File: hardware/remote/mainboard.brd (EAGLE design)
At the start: 34.7 x 20.3 mm, 11 parts, among them J1 AVR_SPI_PRG_6PTH, U1 ATMEGA328P_VQFNVQFN, U2 RFM69HCW

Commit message: Preliminary PCB design
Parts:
- J1: value AVR_SPI_PRG_6PTH -> (none)
- moved C2 11.5 mm to (23.9, 1.52), turned to 180 degrees
- moved C1 10.2 mm to (1.52, 9.65), turned to 270 degrees
- moved R2 5.43 mm to (14.2, 8.13), turned to 90 degrees
- moved C3 1.37 mm to (5.33, 9.65)
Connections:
- removed net N$3: C2.2, U2.10, U2.8
- net GND: now also C2.2, U2.10, U2.8
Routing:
- net VCC: track 0.00 -> 96.7 mm, vias 0 -> 2
- net N$6: track 0.00 -> 38.8 mm, vias 0 -> 4
- net MOSI: track 0.00 -> 33.7 mm, vias 0 -> 2
- net SCK: track 0.00 -> 28.3 mm, vias 0 -> 1
- net N$8: track 0.00 -> 27.9 mm, vias 0 -> 2
- net N$1: track 0.00 -> 20.0 mm
- net MISO: track 0.00 -> 17.0 mm
- net N$2: track 0.00 -> 9.32 mm
- net N$4: track 0.00 -> 2.70 mm
- added copper zone on layer 1, net GND
- added copper zone on layer 16, net GND

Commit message: Added BOM and modified resistor value
Remote
* Added detailed BOM with digikey part numbers.
* Changed R2 from 50k to 47k as 47k is a much more common value.
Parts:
- R2: value 50k -> 47k
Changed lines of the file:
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@@
 <element name="J1" library="SparkFun-Connectors" package="2X3" value="" x="5.08" y="12.7" rot="R90"/>
 <element name="R1" library="SparkFun-Passives" package="0603-RES" value="10k" x="8.128" y="19.05" rot="R180"/>
-<element name="R2" library="SparkFun-Passives" package="0603-RES" value="50k" x="14.224" y="8.128" rot="R90"/>
+<element name="R2" library="SparkFun-Passives" package="0603-RES" value="47k" x="14.224" y="8.128" rot="R90"/>
 <element name="S1" library="SparkFun-Electromechanical" package="TACTILE-PTH" value="" x="4.572" y="4.064">
 <attribute name="PROD_ID" value=" SWCH-08441" x="4.572" y="4.064" size="1.778" layer="27" display="off"/>

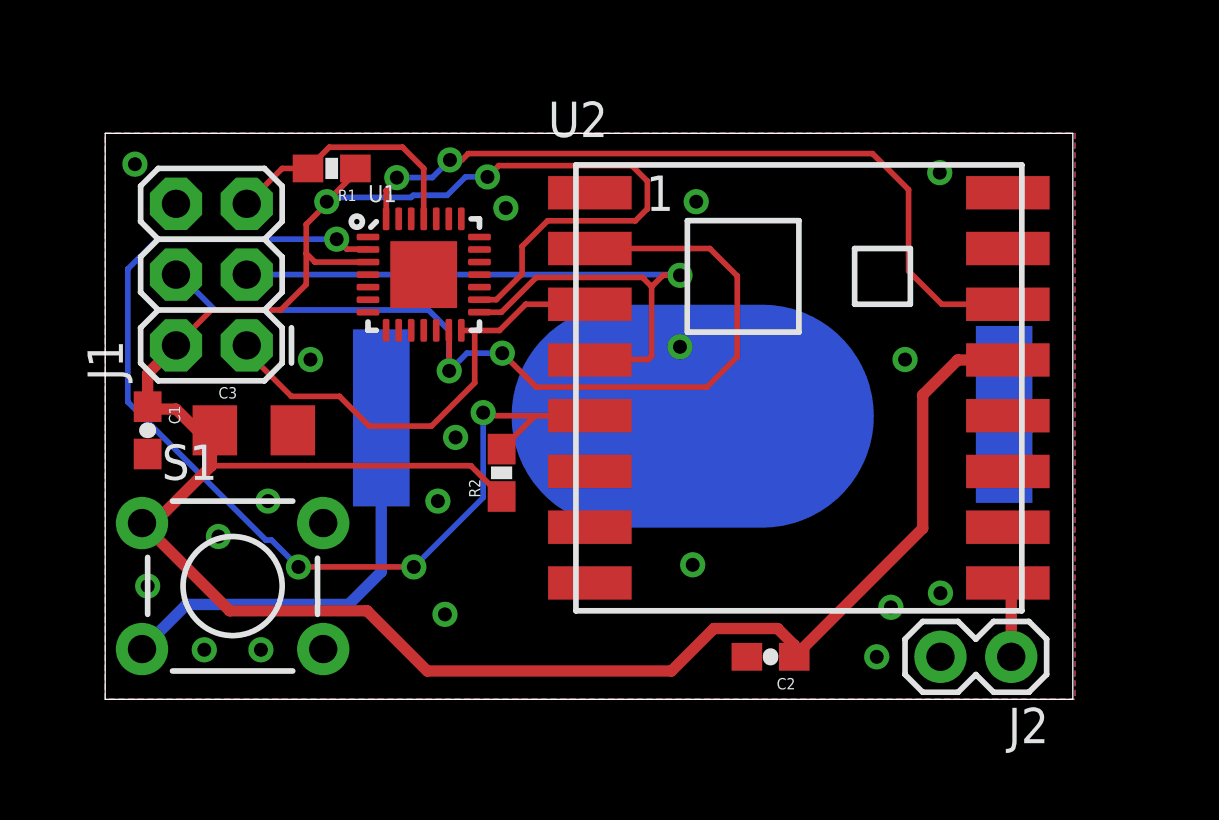
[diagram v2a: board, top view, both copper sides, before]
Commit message: Fixed SPI mismatch
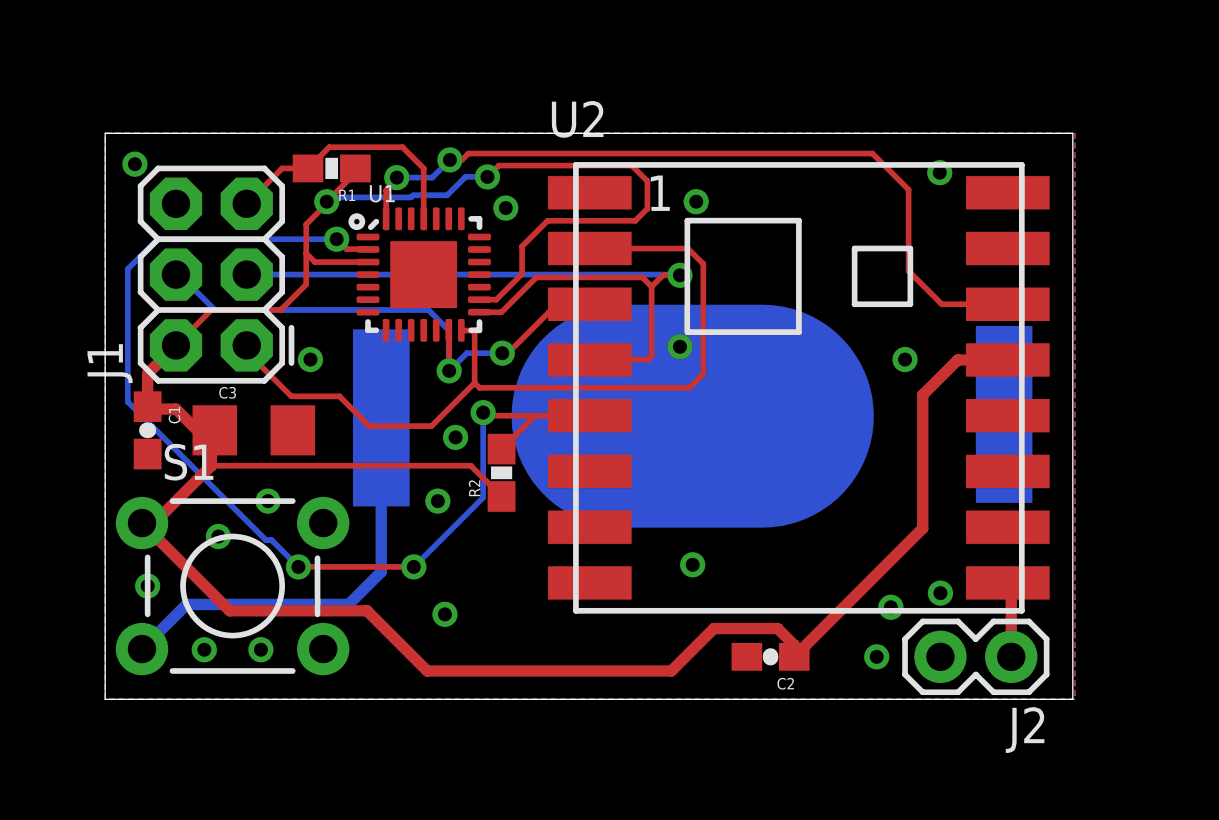
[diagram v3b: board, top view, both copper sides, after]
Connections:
- net MISO: now also U2.2; no longer U2.3
- net MOSI: now also U2.3; no longer U2.2
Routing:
- net MOSI: track 33.7 -> 19.6 mm
- net MISO: track 17.0 -> 29.3 mm
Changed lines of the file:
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@@
 <setting verticaltext="up"/>
 </settings>
-<grid distance="10" unitdist="mil" unit="mil" style="lines" multiple="1" display="no" altdistance="0.025" altunitdist="inch" altunit="inch"/>
+<grid distance="5" unitdist="mil" unit="mil" style="lines" multiple="1" display="no" altdistance="0.025" altunitdist="inch" altunit="inch"/>
 <layers>
 <layer number="1" name="Top" color="4" fill="1" visible="yes" active="yes"/>
@@
 <signal name="MISO">
 <contactref element="U1" pad="14"/>
-<contactref element="U2" pad="3"/>
 <contactref element="J1" pad="1"/>
-<wire x1="17.392" y1="14.176" x2="15.0904" y2="14.176" width="0.2032" layer="1"/>
-<wire x1="15.0904" y1="14.176" x2="14.1478" y2="13.2334" width="0.2032" layer="1"/>
-<wire x1="14.1478" y1="13.2334" x2="13.2842" y2="13.2334" width="0.2032" layer="1"/>
 <wire x1="13.2842" y1="13.2334" x2="12.7866" y2="13.2334" width="0.2032" layer="1"/>
 <wire x1="12.7866" y1="13.2334" x2="12.78" y2="13.24" width="0.2032" layer="1"/>
@@
 <wire x1="13.2588" y1="11.3538" x2="13.2588" y2="13.208" width="0.2032" layer="1"/>
 <wire x1="13.2588" y1="13.208" x2="13.2842" y2="13.2334" width="0.2032" layer="1"/>
+<contactref element="U2" pad="2"/>
+<wire x1="17.392" y1="16.176" x2="20.908" y2="16.176" width="0.2032" layer="1"/>
+<wire x1="20.908" y1="16.176" x2="21.463" y2="15.621" width="0.2032" layer="1"/>
+<wire x1="21.463" y1="15.621" x2="21.463" y2="11.684" width="0.2032" layer="1"/>
+<wire x1="21.463" y1="11.684" x2="20.955" y2="11.176" width="0.2032" layer="1"/>
+<wire x1="20.955" y1="11.176" x2="13.4366" y2="11.176" width="0.2032" layer="1"/>
+<wire x1="13.4366" y1="11.176" x2="13.2588" y2="11.3538" width="0.2032" layer="1"/>
 </signal>
 <signal name="MOSI">
 <contactref element="U1" pad="13"/>
-<contactref element="U2" pad="2"/>
 <contactref element="J1" pad="4"/>
-<wire x1="15.4686" y1="11.2014" x2="14.2494" y2="12.4206" width="0.2032" layer="1"/>
 <via x="14.2494" y="12.4206" extent="1-16" drill="0.5"/>
 <wire x1="14.2494" y1="12.4206" x2="12.9794" y2="12.4206" width="0.2032" layer="16"/>
@@
 <wire x1="12.3444" y1="11.7856" x2="12.3444" y2="13.2256" width="0.2032" layer="1"/>
 <wire x1="12.3444" y1="13.2256" x2="12.33" y2="13.24" width="0.2032" layer="1"/>
-<wire x1="21.59" y1="11.2014" x2="15.4686" y2="11.2014" width="0.2032" layer="1"/>
 <wire x1="2.54" y1="15.24" x2="2.667" y2="15.24" width="0.2032" layer="16"/>
 <wire x1="2.667" y1="15.24" x2="3.937" y2="13.97" width="0.2032" layer="16"/>
@@
 <wire x1="12.33" y1="13.24" x2="12.33" y2="11.8" width="0.2032" layer="16"/>
 <wire x1="12.33" y1="11.8" x2="12.3444" y2="11.7856" width="0.2032" layer="16"/>
-<wire x1="17.392" y1="16.176" x2="21.6954" y2="16.176" width="0.2032" layer="1"/>
-<wire x1="21.6954" y1="16.176" x2="22.6822" y2="15.1892" width="0.2032" layer="1"/>
-<wire x1="22.6822" y1="15.1892" x2="22.6822" y2="12.2936" width="0.2032" layer="1"/>
-<wire x1="22.6822" y1="12.2936" x2="21.59" y2="11.2014" width="0.2032" layer="1"/>
+<contactref element="U2" pad="3"/>
+<wire x1="14.2494" y1="12.4206" x2="14.4526" y2="12.4206" width="0.2032" layer="1"/>
+<wire x1="14.4526" y1="12.4206" x2="16.256" y2="14.224" width="0.2032" layer="1"/>
+<wire x1="16.256" y1="14.224" x2="17.344" y2="14.224" width="0.2032" layer="1"/>
+<wire x1="17.344" y1="14.224" x2="17.392" y2="14.176" width="0.2032" layer="1"/>
 </signal>
 <signal name="N$6">

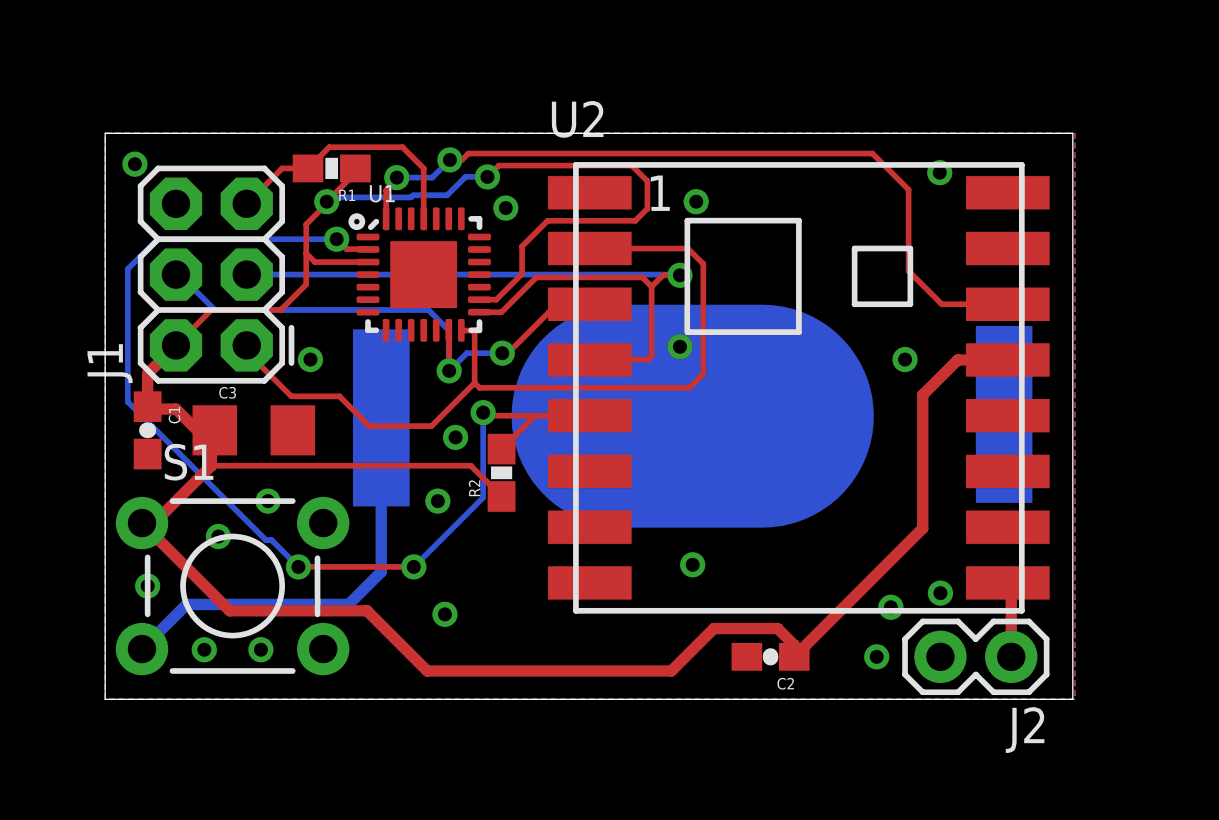
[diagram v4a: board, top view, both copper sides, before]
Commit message: Added SPI series impedance and status LED
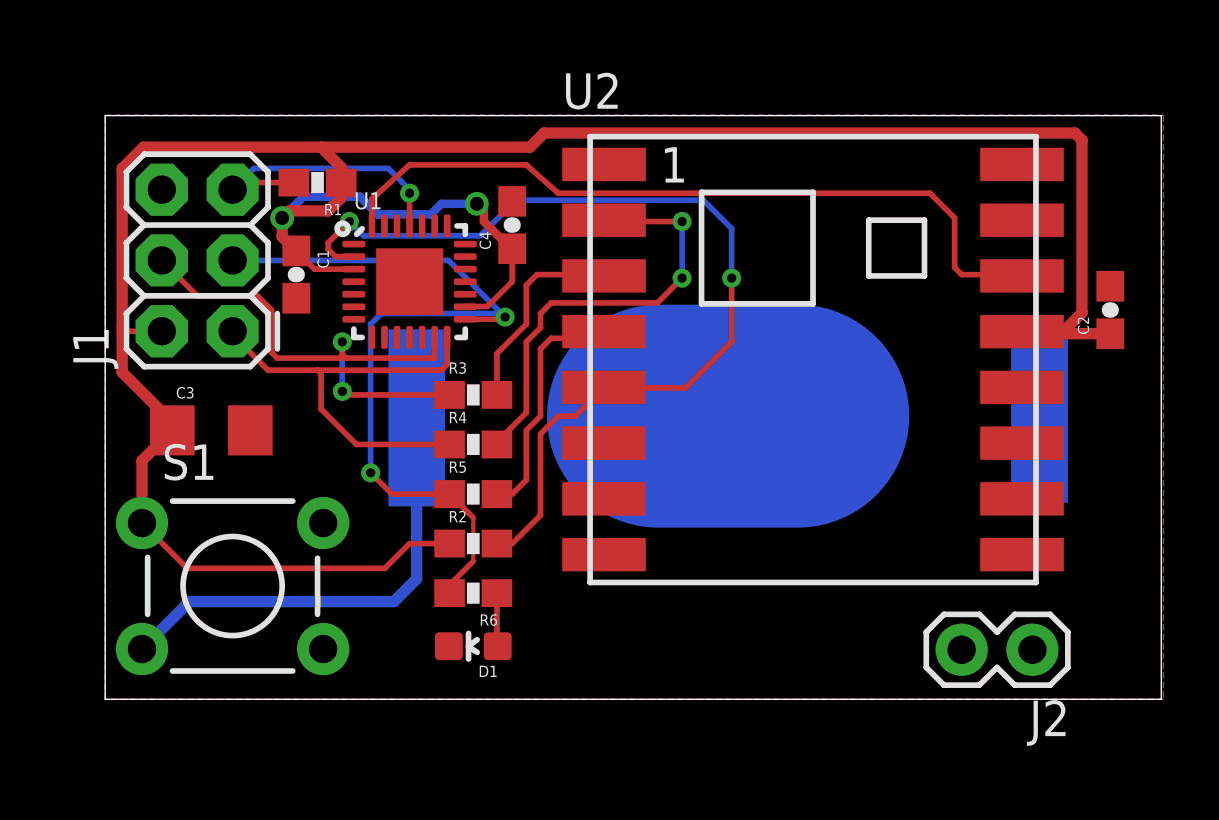
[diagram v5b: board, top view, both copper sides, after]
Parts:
- added C4: 100n, SparkFun-Passives:0603-CAP
- added D1: (no value), SparkFun-LED:LED-0603
- added R3, R4, R5: 330, SparkFun-Passives:0603-RES
- added R6: 180, SparkFun-Passives:0603-RES
- moved C2 17.4 mm to (36.1, 14.0), turned to 90 degrees
- moved C1 7.73 mm to (6.86, 15.2)
- moved R2 2.74 mm to (13.2, 5.59), turned to 0 degrees
- moved C3 1.52 mm to (3.81, 9.65)
- moved BAT1 1.27 mm to (22.4, 10.2)
- moved U2 1.14 mm to (25.4, 12.2)
- moved J2 0.80 mm to (33.3, 1.78)
- moved J1 0.72 mm to (4.57, 13.2)
- moved R1 0.72 mm to (7.62, 18.5)
- moved U1 0.57 mm to (10.9, 15.0)
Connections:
- new net N$3: R3.2, U2.3
- new net N$5: R4.2, U2.2
- new net N$7: R5.2, U2.4
- new net N$9: D1.A, R6.1
- net GND: now also C4.2, D1.C
- net MISO: now also R4.1; no longer U2.2
- net MOSI: now also R3.1; no longer U2.3
- net SCK: now also R5.1, R6.2; no longer U2.4
- net VCC: now also C4.1
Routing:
- net N$5: track 0.00 -> 15.8 mm, vias 0 -> 2
- net MISO: track 29.3 -> 16.0 mm
- net N$7: track 0.00 -> 8.71 mm
- net N$3: track 0.00 -> 7.34 mm
- net N$6: track 38.8 -> 34.4 mm, vias 4 -> 2
- net N$4: track 2.70 -> 0.00 mm
- net N$9: track 0.00 -> 1.92 mm
- net N$1: track 20.0 -> 18.3 mm
- net SCK: track 28.3 -> 29.9 mm, vias 1 -> 2
- net N$2: track 9.32 -> 10.6 mm, vias 0 -> 1
- net VCC: track 96.7 -> 95.8 mm
- net N$8: track 27.9 -> 27.4 mm, vias 2 -> 0
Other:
- board size 34.7 x 20.3 mm -> 37.9 x 20.9 mm
